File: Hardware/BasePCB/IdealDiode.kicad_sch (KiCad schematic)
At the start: 9 parts, among them IC1 LM74704QDDFRQ1, Q7 STD35NF06T4

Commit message: footprint updates
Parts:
- IC1: footprint SOP65P280X110-8N -> LV Carrier Library:LM74704QDDFRQ1
- Q7: footprint STD35NF06T4 -> LV Carrier Library:STD35NF06T4
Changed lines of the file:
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@@
 			)
 		)
-		(property "Footprint" "SOP65P280X110-8N"
+		(property "Footprint" "LV Carrier Library:LM74704QDDFRQ1"
 			(at 57.48 85.09 0)
 			(effects
@@
 			)
 		)
-		(property "Footprint" "STD35NF06T4"
+		(property "Footprint" "LV Carrier Library:STD35NF06T4"
 			(at 51.13 61.595 0)
 			(effects

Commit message: balls ahh layout
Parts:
- removed Q7: STD35NF06T4, LV Carrier Library:STD35NF06T4, symbol STD35NF06T4:STD35NF06T4
- removed TP20, TP25, TP26: TestPoint, TestPoint:TestPoint_THTPad_D3.0mm_Drill1.5mm, symbol Connector:TestPoint
- added Q5: SQJQ140E-T1_GE3, PowerBoardLib:TO200P800X182-5N, symbol PowerBoardLib:SQJQ140E-T1_GE3
- TP27: footprint TestPoint:TestPoint_THTPad_D3.0mm_Drill1.5mm -> TestPoint:TestPoint_Pad_D2.5mm
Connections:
- net DIODE_VIN: now also Q5.2, Q5.3, Q5.4
- net DIODE_VOUT: now also Q5.5
- net at IC1.7 (GATE): now also Q5.1

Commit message: minor silk fixes + gate testpoint
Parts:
- added TP28: TestPoint, TestPoint:TestPoint_Pad_D2.5mm, symbol Connector:TestPoint
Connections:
- net diodeGate: now reaches IC1.7 (GATE), Q5.1
- net diodeGate: now also TP28.1
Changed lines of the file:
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@@
+	)
+	(junction
+		(at 149.86 74.93)
+		(diameter 0)
+		(color 0 0 0 0)
 	)
 	(junction
@@
 	(wire
 		(pts
+			(xy 149.86 74.93) (xy 149.86 81.28)
+		)
+		(stroke
+			(width 0)
+			(type default)
+		)
+	)
+	(wire
+		(pts
 			(xy 142.24 65.405) (xy 147.32 65.405)
 		)
@@
 	(wire
 		(pts
-			(xy 149.86 70.485) (xy 149.86 81.28)
-		)
-		(stroke
-			(width 0)
-			(type default)
-		)
-	)
-	(wire
-		(pts
 			(xy 142.24 65.405) (xy 142.24 78.74)
 		)
@@
 			(width 0)
 			(type default)
+		)
+	)
+	(wire
+		(pts
+			(xy 149.86 70.485) (xy 149.86 74.93)
+		)
+		(stroke
+			(width 0)
+			(type default)
+		)
+	)
+	(label "diodeGate"
+		(at 149.86 74.93 0)
+		(effects
+			(font
+				(size 1.27 1.27)
+			)
+			(justify left bottom)
 		)
 	)
@@
 		)
 	)
+	(symbol
+		(lib_id "Connector:TestPoint")
+		(at 149.86 74.93 90)
+		(unit 1)
+		(exclude_from_sim no)
+		(in_bom yes)
+		(on_board yes)
+		(dnp no)
+		(property "Reference" "TP28"
+			(at 146.685 72.39 90)
+			(effects
+				(font
+					(size 1.27 1.27)
+				)
+			)
+		)
+		(property "Value" "TestPoint"
+			(at 147.8279 72.39 0)
+			(effects
+				(font
+					(size 1.27 1.27)
+				)
+				(justify left)
+				(hide yes)
+			)
+		)
+		(property "Footprint" "TestPoint:TestPoint_Pad_D2.5mm"
+			(at 149.86 69.85 0)
+			(effects
+				(font
+					(size 1.27 1.27)
+				)
+				(hide yes)
+			)
+		)
+		(property "Datasheet" "~"
+			(at 149.86 69.85 0)
+			(effects
+				(font
+					(size 1.27 1.27)
+				)
+				(hide yes)
+			)
+		)
+		(property "Description" "test point"
+			(at 149.86 74.93 0)
+			(effects
+				(font
+					(size 1.27 1.27)
+				)
+				(hide yes)
+			)
+		)
+		(pin "1"
+		)
+		(instances
+			(project "LV Carrier Board"
+				(path "/c5c5922b-1600-4b67-acf3-33264cecd75b/43d57115-5e1b-4cd6-9a42-d8d2dd9ec7f7"
+					(reference "TP28")
+					(unit 1)
+				)
+			)
+		)
+	)

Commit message: fixed some shi
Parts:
- removed C3, C7: 0.1uF, Capacitor_SMD:C_0603_1608Metric_Pad1.08x0.95mm_HandSolder, symbol Device:C
- removed IC1: LM74704QDDFRQ1, LV Carrier Library:LM74704QDDFRQ1, symbol LM74704QDDFRQ1:LM74704QDDFRQ1
- removed TP27, TP28: TestPoint, TestPoint:TestPoint_Pad_D2.5mm, symbol Connector:TestPoint
- added C10, C8: 1 uF, Capacitor_SMD:C_0603_1608Metric, symbol Device:C
- added D26: SMBJ33D, PowerBoardLib:P26_DO-214AA_SMB, symbol PowerBoardLib:SMBJ15D-M3I
- added IC1: AP74502HQTA8-7, LV Carrier Library:AP74502HQTA87, symbol AP74502HQTA8-7:AP74502HQTA8-7
- added Q6: SQJQ140E-T1_GE3, PowerBoardLib:TO200P800X182-5N, symbol PowerBoardLib:SQJQ140E-T1_GE3
- added R1: 160K, Resistor_SMD:R_0603_1608Metric_Pad0.98x0.95mm_HandSolder, symbol Device:R
- added R35: 6.8K, Resistor_SMD:R_0603_1608Metric_Pad0.98x0.95mm_HandSolder, symbol Device:R
- C6: value 10uF -> 0.1 uF; footprint Capacitor_SMD:C_0603_1608Metric_Pad1.08x0.95mm_HandSolder -> Capacitor_SMD:C_0603_1608Metric
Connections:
- net DIODE_EN: now also IC1.1 (EN/UVLO)
- net DIODE_VIN: now also Q5.5, C8.1, D26.2 (A); no longer Q5.2, Q5.3, Q5.4
- net DIODE_VOUT: now also C10.1, Q6.5; no longer C6.2, Q5.5
- net GND: now also C10.2, C8.2, D26.1 (K), IC1.2 (GND), R35.2; no longer C6.1
- net diodeGate renamed GATE
- net GATE: now also IC1.6 (GATE), Q6.1
- new net: C6.2, IC1.4 (VCP)
- new net: IC1.8 (SRC), Q5.2, Q5.3, Q5.4, Q6.2, Q6.3, Q6.4
- new net: IC1.7 (OVLO), R1.2, R35.1
- new net VIN: C6.1, IC1.5 (VIN), R1.1
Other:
- note added: "OV Resistor Divider: OV = VIN (R35 / (R1 + R35)) = 30.662 V"
- note removed: "Ccap must be 10x Ciss for NMOS Ciss for NMOS is 1300pF Minimum 0.1uF"
- note removed: "FETGOOD has max output of 1mA (no led), and pulls low when a fault has occurred"
- note removed: "Input cap 22nF minimum"
- note removed: "LV_EN_PS low = PS, therefore high = Supp"
- note removed: "Output cap 100nF minimum"
- note removed: "When EN > 2.5V NMOS is driven, EN is 60V tolerant"

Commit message: donut daddy
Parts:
- removed Q5, Q6: SQJQ140E-T1_GE3, PowerBoardLib:TO200P800X182-5N, symbol PowerBoardLib:SQJQ140E-T1_GE3
- added Q5, Q8: NVMFWS1D7N04XMT1G, LV Carrier Library:NVMFWS3D0P04M8LT1G, symbol NVMFWS1D7N04XMT1G:NVMFWS1D7N04XMT1G
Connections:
- net DIODE_VIN: now also Q5.5, Q5.6, Q5.7, Q5.8, Q5.9
- net DIODE_VOUT: now also Q8.5, Q8.6, Q8.7, Q8.8, Q8.9
- net GATE: now also Q5.4, Q8.4
- net at IC1.8 (SRC): now also Q5.1, Q5.2, Q5.3, Q8.1, Q8.2, Q8.3
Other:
- moved on the sheet: C10, C8, D26, R1, R35

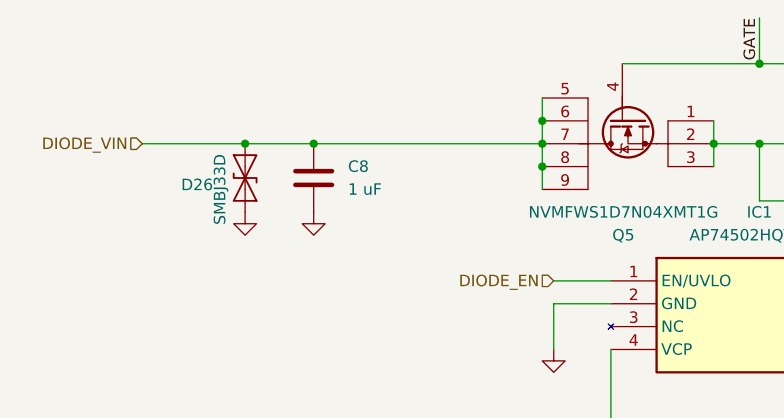
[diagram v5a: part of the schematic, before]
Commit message: negative logic switches fix
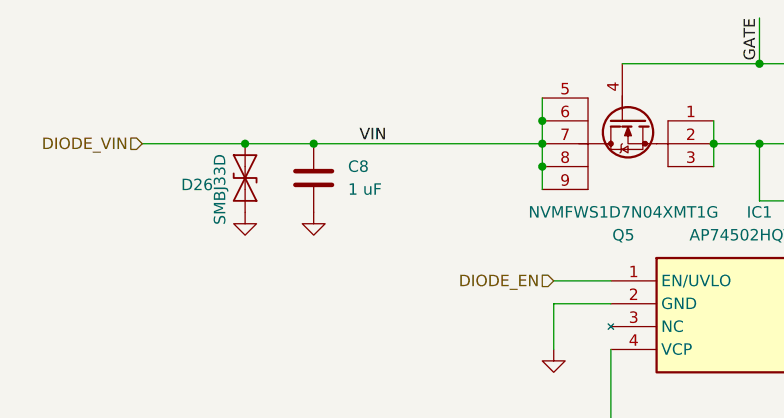
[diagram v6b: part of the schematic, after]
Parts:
- C10, C6, C8: footprint Capacitor_SMD:C_0603_1608Metric -> Capacitor_SMD:C_0603_1608Metric_Pad1.08x0.95mm_HandSolder
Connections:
- net VIN is gone; now on net DIODE_VIN: C6.1, IC1.5 (VIN), R1.1
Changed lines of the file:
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@@
+		)
+	)
+	(label "VIN"
+		(at 104.14 83.82 0)
+		(effects
+			(font
+				(size 1.27 1.27)
+			)
+			(justify left bottom)
 		)
 	)
@@
 			)
 		)
-		(property "Footprint" "Capacitor_SMD:C_0603_1608Metric"
+		(property "Footprint" "Capacitor_SMD:C_0603_1608Metric_Pad1.08x0.95mm_HandSolder"
 			(at 168.6052 114.3 0)
 			(effects
@@
 			)
 		)
-		(property "Footprint" "Capacitor_SMD:C_0603_1608Metric"
+		(property "Footprint" "Capacitor_SMD:C_0603_1608Metric_Pad1.08x0.95mm_HandSolder"
 			(at 100.0252 91.44 0)
 			(effects
@@
 			)
 		)
-		(property "Footprint" "Capacitor_SMD:C_0603_1608Metric"
+		(property "Footprint" "Capacitor_SMD:C_0603_1608Metric_Pad1.08x0.95mm_HandSolder"
 			(at 185.1152 91.44 0)
 			(effects

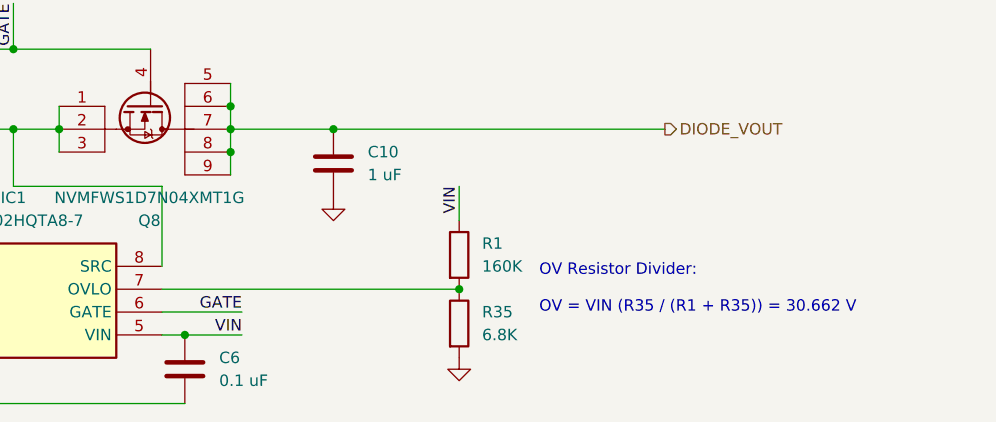
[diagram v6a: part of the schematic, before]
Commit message: change OV and fix silk
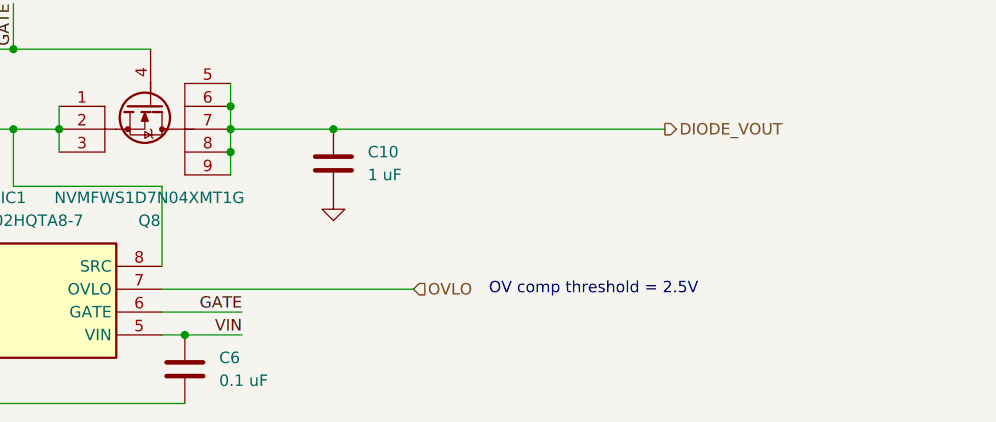
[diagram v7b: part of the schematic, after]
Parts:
- removed R1: 160K, Resistor_SMD:R_0603_1608Metric_Pad0.98x0.95mm_HandSolder, symbol Device:R
- removed R35: 6.8K, Resistor_SMD:R_0603_1608Metric_Pad0.98x0.95mm_HandSolder, symbol Device:R
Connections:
- net OVLO: now reaches IC1.7 (OVLO)
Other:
- note added: "OV comp threshold = 2.5V"
- note removed: "OV Resistor Divider: OV = VIN (R35 / (R1 + R35)) = 30.662 V"
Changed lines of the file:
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@@
 	(generator_version "9.0")
 	(paper "A4")
-	(text "OV Resistor Divider:\n\nOV = VIN (R35 / (R1 + R35)) = 30.662 V"
+	(text "OV comp threshold = 2.5V"
 		(exclude_from_sim no)
-		(at 207.01 101.6 0)
+		(at 201.422 101.6 0)
 		(effects
 			(font
@@
 	)
 	(junction
-		(at 198.12 101.6)
-		(diameter 0)
-		(color 0 0 0 0)
-	)
-	(junction
 		(at 172.72 86.36)
 		(diameter 0)
@@
 	(wire
 		(pts
-			(xy 198.12 90.17) (xy 198.12 93.98)
-		)
-		(stroke
-			(width 0)
-			(type default)
-		)
-	)
-	(wire
-		(pts
 			(xy 148.59 69.85) (xy 148.59 74.93)
 		)
@@
 	(wire
 		(pts
-			(xy 165.1 101.6) (xy 198.12 101.6)
-		)
-		(stroke
-			(width 0)
-			(type default)
-		)
-	)
-	(wire
-		(pts
 			(xy 173.99 106.68) (xy 167.64 106.68)
 		)
@@
 		(pts
 			(xy 184.15 83.82) (xy 220.98 83.82)
+		)
+		(stroke
+			(width 0)
+			(type default)
+		)
+	)
+	(wire
+		(pts
+			(xy 165.1 101.6) (xy 193.04 101.6)
 		)
 		(stroke
@@
 		)
 	)
-	(label "VIN"
-		(at 198.12 90.17 270)
+	(hierarchical_label "OVLO"
+		(shape input)
+		(at 193.04 101.6 0)
 		(effects
 			(font
 				(size 1.27 1.27)
 			)
-			(justify right bottom)
+			(justify left)
 		)
 	)
@@
 	)
 	(symbol
-		(lib_id "power:GND")
-		(at 198.12 109.22 0)
-		(unit 1)
-		(exclude_from_sim no)
-		(in_bom yes)
-		(on_board yes)
-		(dnp no)
-		(fields_autoplaced yes)
-		(property "Reference" "#PWR046"
-			(at 198.12 115.57 0)
-			(effects
-				(font
-					(size 1.27 1.27)
-				)
-				(hide yes)
-			)
-		)
-		(property "Value" "GND"
-			(at 198.12 114.3 0)
-			(effects
-				(font
-					(size 1.27 1.27)
-				)
-				(hide yes)
-			)
-		)
-		(property "Footprint" ""
-			(at 198.12 109.22 0)
-			(effects
-				(font
-					(size 1.27 1.27)
-				)
-				(hide yes)
-			)
-		)
-		(property "Datasheet" ""
-			(at 198.12 109.22 0)
-			(effects
-				(font
-					(size 1.27 1.27)
-				)
-				(hide yes)
-			)
-		)
-		(property "Description" "Power symbol creates a global label with name \"GND\" , ground"
-			(at 198.12 109.22 0)
-			(effects
-				(font
-					(size 1.27 1.27)
-				)
-				(hide yes)
-			)
-		)
-		(pin "1"
-		)
-		(instances
-			(project "LV Carrier Board"
-				(path "/c5c5922b-1600-4b67-acf3-33264cecd75b/43d57115-5e1b-4cd6-9a42-d8d2dd9ec7f7"
-					(reference "#PWR047")
-					(unit 1)
-				)
-				(path "/c5c5922b-1600-4b67-acf3-33264cecd75b/d4cbd764-e723-45ee-b4b7-e620455af31e/235a5f78-79bc-442b-9f8f-94d7d41f7629"
-					(reference "#PWR046")
-					(unit 1)
-				)
-			)
-		)
-	)
-	(symbol
-		(lib_id "Device:R")
-		(at 198.12 97.79 0)
-		(unit 1)
-		(exclude_from_sim no)
-		(in_bom yes)
-		(on_board yes)
-		(dnp no)
-		(fields_autoplaced yes)
-		(property "Reference" "R1"
-			(at 200.66 96.5199 0)
-			(effects
-				(font
-					(size 1.27 1.27)
-				)
-				(justify left)
-			)
-		)
-		(property "Value" "160K"
-			(at 200.66 99.0599 0)
-			(effects
-				(font
-					(size 1.27 1.27)
-				)
-				(justify left)
-			)
-		)
-		(property "Footprint" "Resistor_SMD:R_0603_1608Metric_Pad0.98x0.95mm_HandSolder"
-			(at 196.342 97.79 90)
-			(effects
-				(font
-					(size 1.27 1.27)
-				)
-				(hide yes)
-			)
-		)
-		(property "Datasheet" "~"
-			(at 198.12 97.79 0)
-			(effects
-				(font
-					(size 1.27 1.27)
-				)
-				(hide yes)
-			)
-		)
-		(property "Description" "Resistor"
-			(at 198.12 97.79 0)
-			(effects
-				(font
-					(size 1.27 1.27)
-				)
-				(hide yes)
-			)
-		)
-		(pin "2"
-		)
-		(pin "1"
-		)
-		(instances
-			(project ""
-				(path "/c5c5922b-1600-4b67-acf3-33264cecd75b/43d57115-5e1b-4cd6-9a42-d8d2dd9ec7f7"
-					(reference "R19")
-					(unit 1)
-				)
-				(path "/c5c5922b-1600-4b67-acf3-33264cecd75b/d4cbd764-e723-45ee-b4b7-e620455af31e/235a5f78-79bc-442b-9f8f-94d7d41f7629"
-					(reference "R1")
-					(unit 1)
-				)
-			)
-		)
-	)
-	(symbol
 		(lib_id "PowerBoardLib:SMBJ15D-M3I")
 		(at 91.44 87.63 90)
@@
 					(unit 1)
 				)
-			)
-		)
-	)
-	(symbol
-		(lib_id "Device:R")
-		(at 198.12 105.41 0)
-		(unit 1)
-		(exclude_from_sim no)
-		(in_bom yes)
-		(on_board yes)
-		(dnp no)
-		(fields_autoplaced yes)
-		(property "Reference" "R35"
-			(at 200.66 104.1399 0)
-			(effects
-				(font
-					(size 1.27 1.27)
-				)
-				(justify left)
-			)
-		)
-		(property "Value" "6.8K"
-			(at 200.66 106.6799 0)
-			(effects
-				(font
-					(size 1.27 1.27)
-				)
-				(justify left)
-			)
-		)
-		(property "Footprint" "Resistor_SMD:R_0603_1608Metric_Pad0.98x0.95mm_HandSolder"
-			(at 196.342 105.41 90)
-			(effects
-				(font
-					(size 1.27 1.27)
-				)
-				(hide yes)
-			)
-		)
-		(property "Datasheet" "~"
-			(at 198.12 105.41 0)
-			(effects
-				(font
-					(size 1.27 1.27)
-				)
-				(hide yes)
-			)
-		)
-		(property "Description" "Resistor"
-			(at 198.12 105.41 0)
-			(effects
-				(font
-					(size 1.27 1.27)
-				)
-				(hide yes)
-			)
-		)
-		(pin "2"
-		)
-		(pin "1"
-		)
-		(instances
-			(project "LV Carrier Board"
-				(path "/c5c5922b-1600-4b67-acf3-33264cecd75b/43d57115-5e1b-4cd6-9a42-d8d2dd9ec7f7"
-					(reference "R39")
-					(unit 1)
-				)
-				(path "/c5c5922b-1600-4b67-acf3-33264cecd75b/d4cbd764-e723-45ee-b4b7-e620455af31e/235a5f78-79bc-442b-9f8f-94d7d41f7629"
-					(reference "R35")
-					(unit 1)
-				)

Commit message: BOM
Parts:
- C10, C8: P/N (none) -> MLASU168SB5105KTNA01
- C6: P/N (none) -> MLASH168SB7104KTNA01
- IC1: P/N (none) -> AP74502HQTA8-7
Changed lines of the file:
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@@
+			)
+		)
+		(property "P/N" "MLASH168SB7104KTNA01"
+			(at 167.64 110.49 0)
+			(effects
+				(font
+					(size 1.27 1.27)
+				)
 			)
 		)
@@
 			)
 		)
+		(property "P/N" "AP74502HQTA8-7"
+			(at 132.08 99.06 0)
+			(effects
+				(font
+					(size 1.27 1.27)
+				)
+			)
+		)
 		(pin "3"
 		)
@@
 			)
 		)
+		(property "P/N" "MLASU168SB5105KTNA01"
+			(at 99.06 87.63 0)
+			(effects
+				(font
+					(size 1.27 1.27)
+				)
+			)
+		)
 		(pin "1"
 		)
@@
 			)
 		)
+		(property "P/N" "MLASU168SB5105KTNA01"
+			(at 184.15 87.63 0)
+			(effects
+				(font
+					(size 1.27 1.27)
+				)
+			)
+		)
